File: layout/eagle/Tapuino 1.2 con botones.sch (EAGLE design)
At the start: 12 parts, among them CN1 C64_CASETTE_EDGE, IC1 4052N, IC2 ARDUINO_NANO_V3

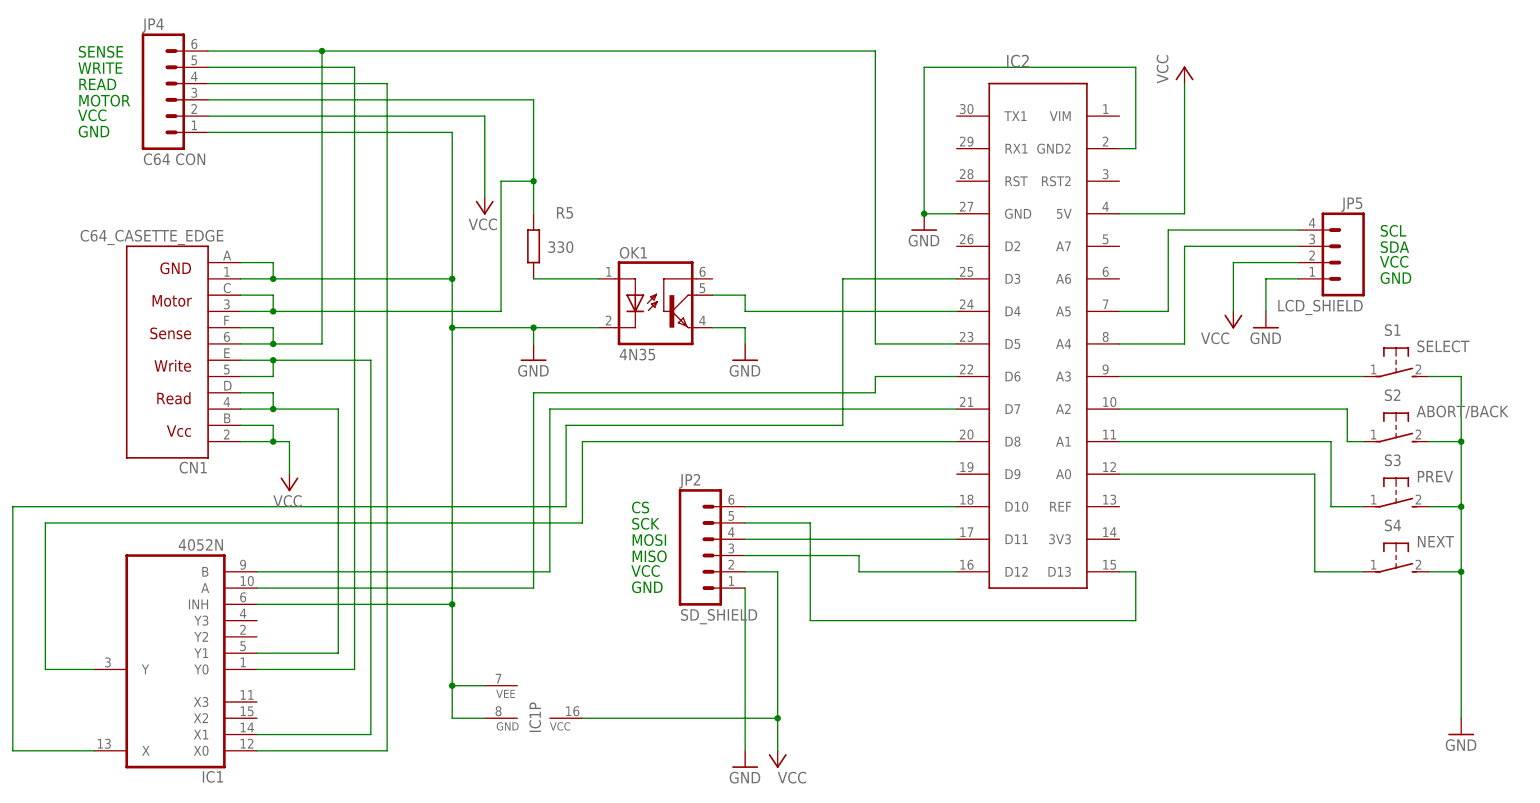
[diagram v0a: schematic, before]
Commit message: Added spcbm 1.2 board, removed mine
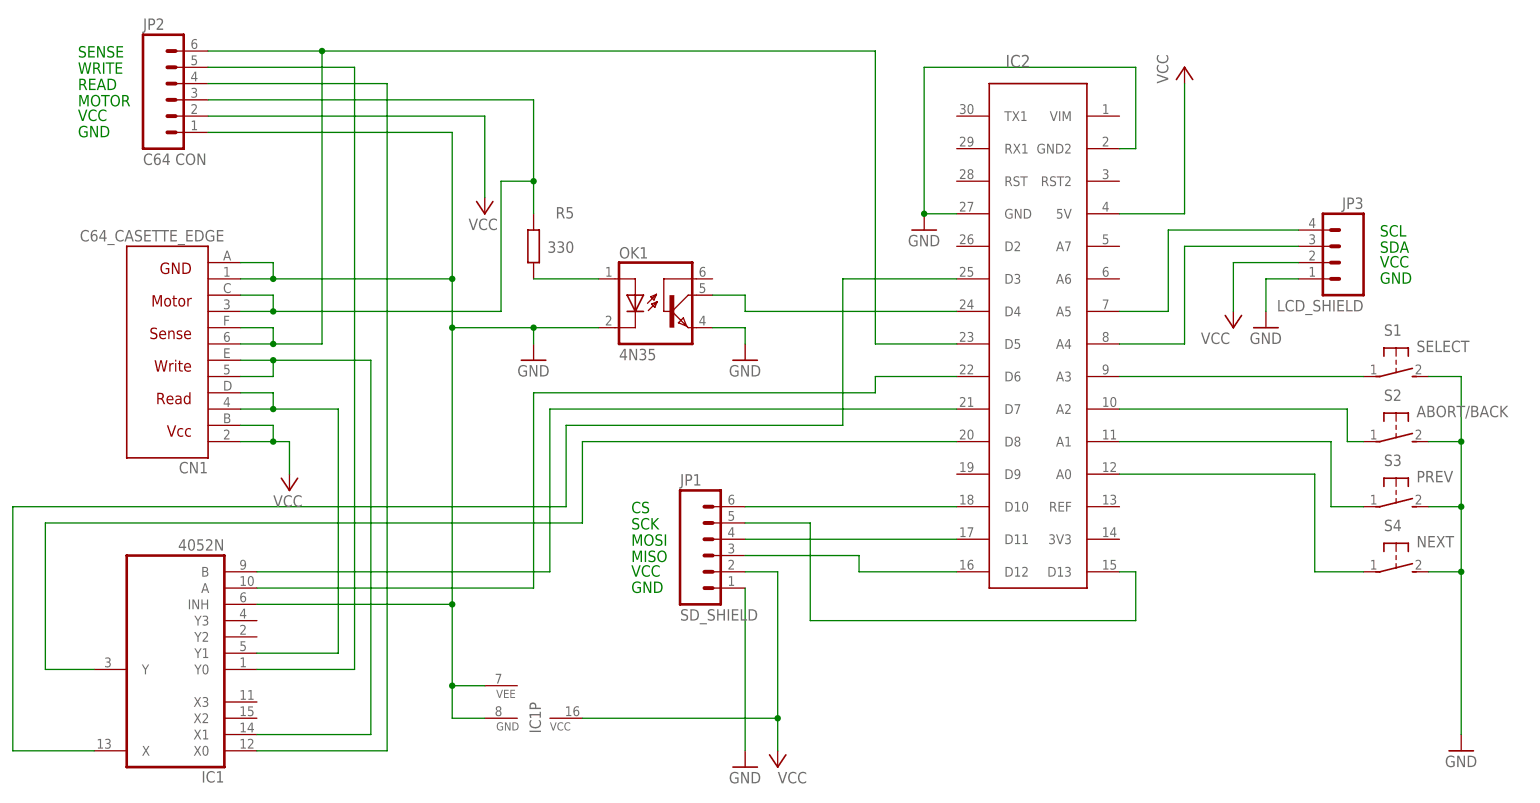
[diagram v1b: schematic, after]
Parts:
- removed JP4: C64 CON, SparkFun:M06LOCK_LONGPADS
- added JP1: SD_SHIELD, SparkFun:M06LOCK_LONGPADS
- CN1: device commodore:C64_CASETTE_EDGE -> commodore MOD:C64_CASETTE_EDGE
- JP2: value SD_SHIELD -> C64 CON
- renumbered JP5 to JP3
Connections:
- net GND: now also JP1.1; no longer JP4.1
- net N$1: now also JP1.3; no longer JP2.3
- net N$13: now also JP2.5; no longer JP4.5
- net N$14: now also JP2.3; no longer JP4.3
- net N$16: now also JP2.4; no longer JP4.4
- net N$17: now also JP2.6; no longer JP4.6
- net N$2: now also JP1.6; no longer JP2.6
- net N$3: now also JP1.5; no longer JP2.5
- net N$4: now also JP1.4; no longer JP2.4
- net VCC: now also JP1.2; no longer JP4.2
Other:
- moved on the sheet: JP2
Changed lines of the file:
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@@
 <part name="P+2" library="supply1" deviceset="VCC" device=""/>
 <part name="P+3" library="supply1" deviceset="VCC" device=""/>
-<part name="CN1" library="commodore" deviceset="C64_CASETTE_EDGE" device=""/>
+<part name="CN1" library="commodore MOD" deviceset="C64_CASETTE_EDGE" device=""/>
 <part name="R5" library="resistor" deviceset="R-EU_" device="0207/10" value="330"/>
 <part name="GND4" library="supply1" deviceset="GND" device=""/>
@@
 <part name="P+4" library="supply1" deviceset="VCC" device=""/>
 <part name="P+6" library="supply1" deviceset="VCC" device=""/>
-<part name="JP2" library="SparkFun" deviceset="M06" device="LOCK_LONGPADS" value="SD_SHIELD"/>
+<part name="JP1" library="SparkFun" deviceset="M06" device="LOCK_LONGPADS" value="SD_SHIELD"/>
 <part name="OK1" library="optocoupler" deviceset="4N35" device=""/>
-<part name="JP4" library="SparkFun" deviceset="M06" device="LOCK_LONGPADS" value="C64 CON"/>
-<part name="JP5" library="SparkFun" deviceset="M04" device="LOCK_LONGPADS" value="LCD_SHIELD"/>
+<part name="JP2" library="SparkFun" deviceset="M06" device="LOCK_LONGPADS" value="C64 CON"/>
+<part name="JP3" library="SparkFun" deviceset="M04" device="LOCK_LONGPADS" value="LCD_SHIELD"/>
 <part name="IC2" library="arduino" deviceset="ARDUINO_NANO_V3" device=""/>
 <part name="S1" library="switch-omron" deviceset="31-XX" device="" value="SELECT"/>
@@
 </instance>
 <instance part="IC1" gate="P" x="-7.62" y="-7.62" rot="R270"/>
-<instance part="JP2" gate="G$1" x="20.32" y="17.78"/>
+<instance part="JP1" gate="G$1" x="20.32" y="17.78"/>
 <instance part="OK1" gate="G$1" x="12.7" y="58.42"/>
-<instance part="JP4" gate="G$1" x="-63.5" y="88.9"/>
-<instance part="JP5" gate="G$1" x="116.84" y="63.5" rot="MR0"/>
+<instance part="JP2" gate="G$1" x="-63.5" y="88.9"/>
+<instance part="JP3" gate="G$1" x="116.84" y="63.5" rot="MR0"/>
 <instance part="IC2" gate="G$1" x="68.58" y="78.74"/>
 <instance part="S1" gate="1" x="127" y="45.72" rot="R270"/>
@@
 <instance part="S4" gate="1" x="127" y="15.24" rot="R270"/>
 <instance part="GND6" gate="1" x="53.34" y="68.58"/>
-<instance part="GND1" gate="1" x="137.16" y="-10.16"/>
+<instance part="GND1" gate="1" x="137.16" y="-12.7"/>
 </instances>
 <busses>
@@
 <wire x1="25.4" y1="17.78" x2="43.18" y2="17.78" width="0.1524" layer="91"/>
 <wire x1="43.18" y1="17.78" x2="43.18" y2="15.24" width="0.1524" layer="91"/>
-<pinref part="JP2" gate="G$1" pin="3"/>
+<pinref part="JP1" gate="G$1" pin="3"/>
 <pinref part="IC2" gate="G$1" pin="D12"/>
 <wire x1="43.18" y1="15.24" x2="58.42" y2="15.24" width="0.1524" layer="91"/>
@@
 <wire x1="86.36" y1="7.62" x2="86.36" y2="15.24" width="0.1524" layer="91"/>
 <wire x1="86.36" y1="15.24" x2="83.82" y2="15.24" width="0.1524" layer="91"/>
-<pinref part="JP2" gate="G$1" pin="5"/>
+<pinref part="JP1" gate="G$1" pin="5"/>
 <pinref part="IC2" gate="G$1" pin="D13"/>
 </segment>
@@
 <wire x1="91.44" y1="55.88" x2="91.44" y2="68.58" width="0.1524" layer="91"/>
 <wire x1="91.44" y1="68.58" x2="111.76" y2="68.58" width="0.1524" layer="91"/>
-<pinref part="JP5" gate="G$1" pin="4"/>
+<pinref part="JP3" gate="G$1" pin="4"/>
 <pinref part="IC2" gate="G$1" pin="A5"/>
 </segment>
@@
 <wire x1="93.98" y1="50.8" x2="93.98" y2="66.04" width="0.1524" layer="91"/>
 <wire x1="93.98" y1="66.04" x2="111.76" y2="66.04" width="0.1524" layer="91"/>
-<pinref part="JP5" gate="G$1" pin="3"/>
+<pinref part="JP3" gate="G$1" pin="3"/>
 <pinref part="IC2" gate="G$1" pin="A4"/>
 </segment>
@@
 <wire x1="106.68" y1="60.96" x2="111.76" y2="60.96" width="0.1524" layer="91"/>
 <pinref part="GND3" gate="1" pin="GND"/>
-<pinref part="JP5" gate="G$1" pin="1"/>
+<pinref part="JP3" gate="G$1" pin="1"/>
 </segment>
 <segment>
@@
 <wire x1="-50.8" y1="10.16" x2="-20.32" y2="10.16" width="0.1524" layer="91"/>
 <junction x="-20.32" y="10.16"/>
-<pinref part="JP4" gate="G$1" pin="1"/>
+<pinref part="JP2" gate="G$1" pin="1"/>
 <wire x1="-20.32" y1="53.34" x2="-7.62" y2="53.34" width="0.1524" layer="91"/>
 <junction x="-20.32" y="53.34"/>
@@
 </segment>
 <segment>
+<pinref part="JP1" gate="G$1" pin="1"/>
 <pinref part="GND2" gate="1" pin="GND"/>
-<pinref part="JP2" gate="G$1" pin="1"/>
 <wire x1="25.4" y1="12.7" x2="25.4" y2="-12.7" width="0.1524" layer="91"/>
 </segment>
@@
 </segment>
 <segment>
-<pinref part="S4" gate="1" pin="S"/>
 <wire x1="137.16" y1="45.72" x2="137.16" y2="35.56" width="0.1524" layer="91"/>
 <wire x1="137.16" y1="35.56" x2="137.16" y2="25.4" width="0.1524" layer="91"/>
-<wire x1="137.16" y1="25.4" x2="137.16" y2="15.24" width="0.1524" layer="91"/>
-<wire x1="137.16" y1="15.24" x2="132.08" y2="15.24" width="0.1524" layer="91"/>
 <pinref part="S3" gate="1" pin="S"/>
 <wire x1="132.08" y1="25.4" x2="137.16" y2="25.4" width="0.1524" layer="91"/>
@@
 <junction x="137.16" y="35.56"/>
 <junction x="137.16" y="25.4"/>
-<wire x1="137.16" y1="-7.62" x2="137.16" y2="15.24" width="0.1524" layer="91"/>
+<wire x1="137.16" y1="25.4" x2="137.16" y2="15.24" width="0.1524" layer="91"/>
+<pinref part="GND1" gate="1" pin="GND"/>
+<pinref part="S4" gate="1" pin="S"/>
+<wire x1="137.16" y1="15.24" x2="137.16" y2="-10.16" width="0.1524" layer="91"/>
+<wire x1="132.08" y1="15.24" x2="137.16" y2="15.24" width="0.1524" layer="91"/>
 <junction x="137.16" y="15.24"/>
-<pinref part="GND1" gate="1" pin="GND"/>
 </segment>
 </net>
@@
 <wire x1="0" y1="-7.62" x2="30.48" y2="-7.62" width="0.1524" layer="91"/>
 <junction x="30.48" y="-7.62"/>
-<pinref part="JP2" gate="G$1" pin="2"/>
+<pinref part="JP1" gate="G$1" pin="2"/>
 </segment>
 <segment>
@@
 <wire x1="101.6" y1="63.5" x2="111.76" y2="63.5" width="0.1524" layer="91"/>
 <pinref part="P+3" gate="VCC" pin="VCC"/>
-<pinref part="JP5" gate="G$1" pin="2"/>
+<pinref part="JP3" gate="G$1" pin="2"/>
 </segment>
 <segment>
@@
 <wire x1="-15.24" y1="86.36" x2="-15.24" y2="73.66" width="0.1524" layer="91"/>
 <pinref part="P+4" gate="VCC" pin="VCC"/>
-<pinref part="JP4" gate="G$1" pin="2"/>
+<pinref part="JP2" gate="G$1" pin="2"/>
 </segment>
 <segment>
@@
 <wire x1="-48.26" y1="58.42" x2="-48.26" y2="55.88" width="0.1524" layer="91"/>
 <junction x="-48.26" y="55.88"/>
-<pinref part="JP4" gate="G$1" pin="3"/>
+<pinref part="JP2" gate="G$1" pin="3"/>
 </segment>
 </net>
@@
 <pinref part="IC1" gate="A" pin="X0"/>
 <wire x1="-30.48" y1="-12.7" x2="-50.8" y2="-12.7" width="0.1524" layer="91"/>
-<pinref part="JP4" gate="G$1" pin="4"/>
+<pinref part="JP2" gate="G$1" pin="4"/>
 </segment>
 </net>
@@
 <wire x1="-48.26" y1="53.34" x2="-48.26" y2="50.8" width="0.1524" layer="91"/>
 <junction x="-48.26" y="50.8"/>
-<pinref part="JP4" gate="G$1" pin="6"/>
+<pinref part="JP2" gate="G$1" pin="6"/>
 <pinref part="IC2" gate="G$1" pin="D5"/>
 <wire x1="45.72" y1="50.8" x2="58.42" y2="50.8" width="0.1524" layer="91"/>
@@
 <pinref part="IC1" gate="A" pin="Y0"/>
 <wire x1="-35.56" y1="0" x2="-50.8" y2="0" width="0.1524" layer="91"/>
-<pinref part="JP4" gate="G$1" pin="5"/>
+<pinref part="JP2" gate="G$1" pin="5"/>
 </segment>
 </net>
@@
 <net name="N$2" class="0">
 <segment>
-<pinref part="JP2" gate="G$1" pin="6"/>
+<pinref part="JP1" gate="G$1" pin="6"/>
 <pinref part="IC2" gate="G$1" pin="D10"/>
 <wire x1="25.4" y1="25.4" x2="58.42" y2="25.4" width="0.1524" layer="91"/>
@@
 <net name="N$4" class="0">
 <segment>
-<pinref part="JP2" gate="G$1" pin="4"/>
+<pinref part="JP1" gate="G$1" pin="4"/>
 <pinref part="IC2" gate="G$1" pin="D11"/>
 <wire x1="25.4" y1="20.32" x2="58.42" y2="20.32" width="0.1524" layer="91"/>
